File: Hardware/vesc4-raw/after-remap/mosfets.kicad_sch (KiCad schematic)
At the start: 15 parts, among them Q1 IPT007N06NATMA1, Q2 IPT007N06NATMA1, Q3 IPT007N06NATMA1, Q4 IPT007N06NATMA1, Q5 IPT007N06NATMA1, Q6 IPT007N06NATMA1

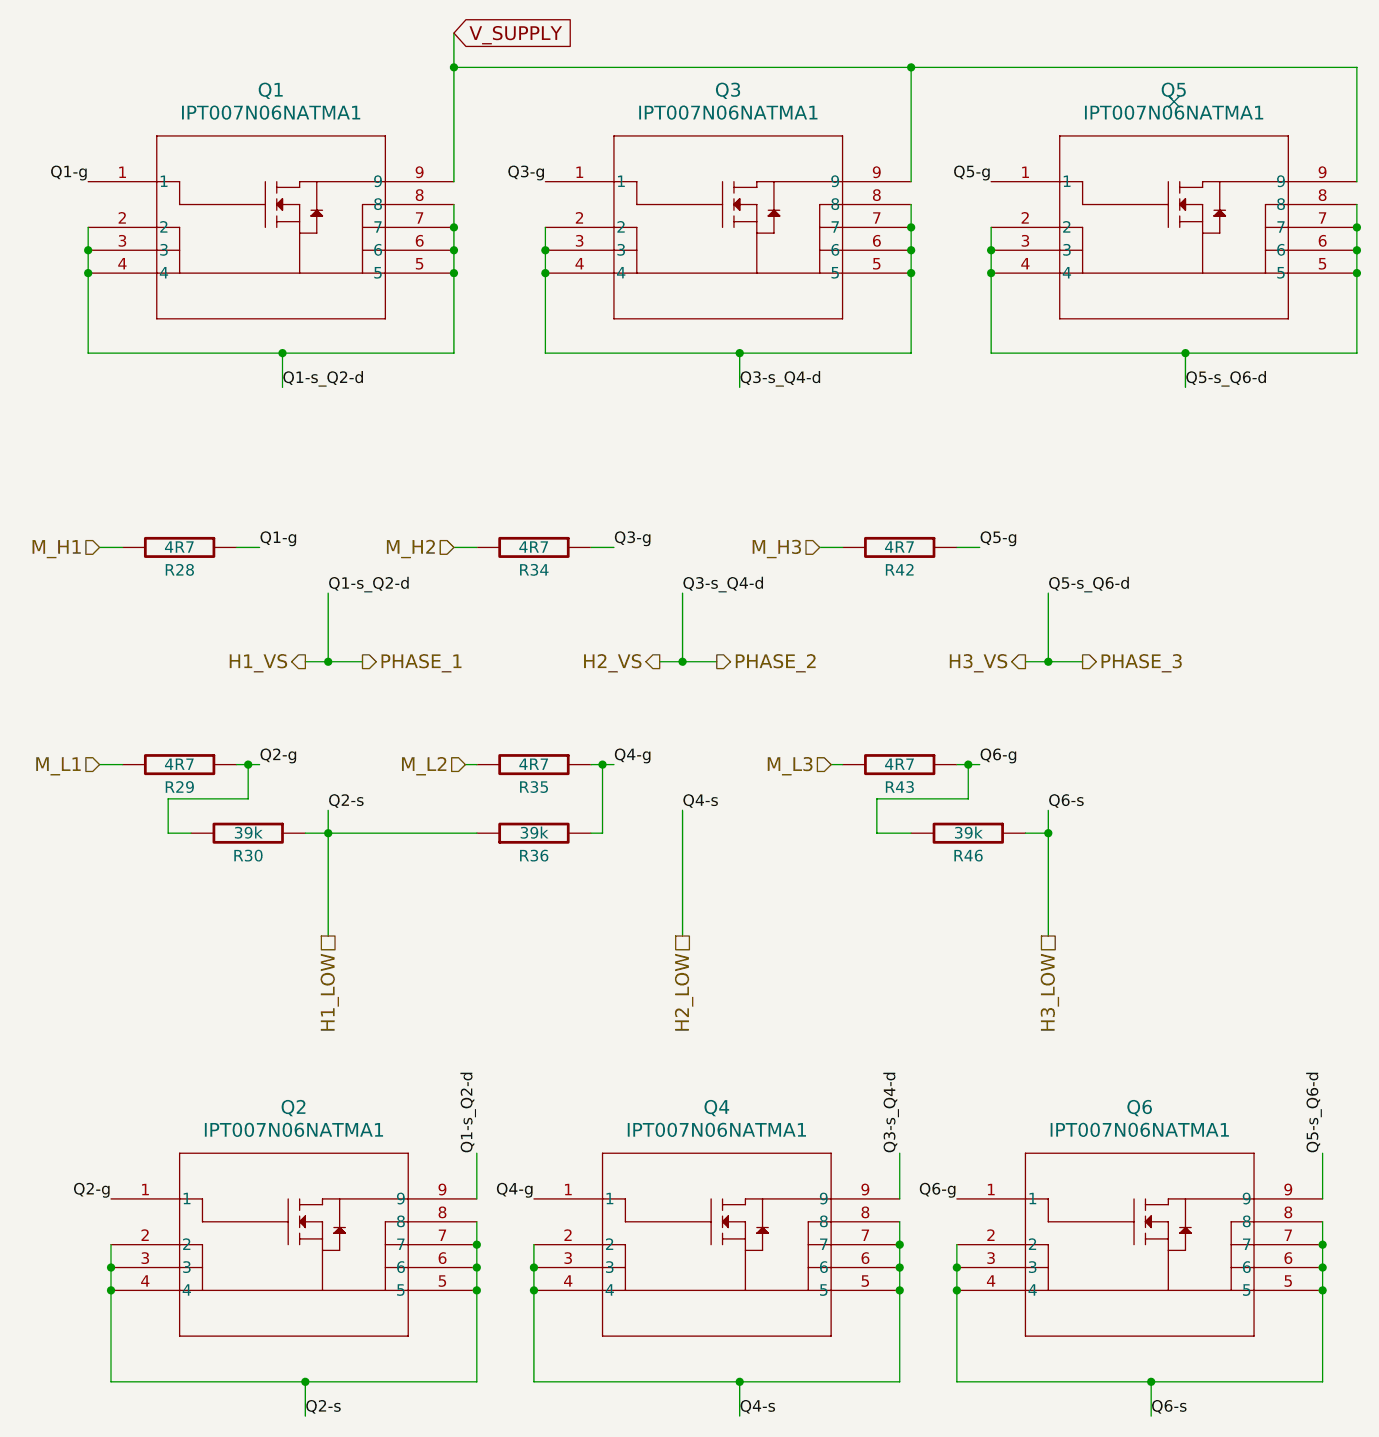
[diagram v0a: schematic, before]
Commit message: update mosfet
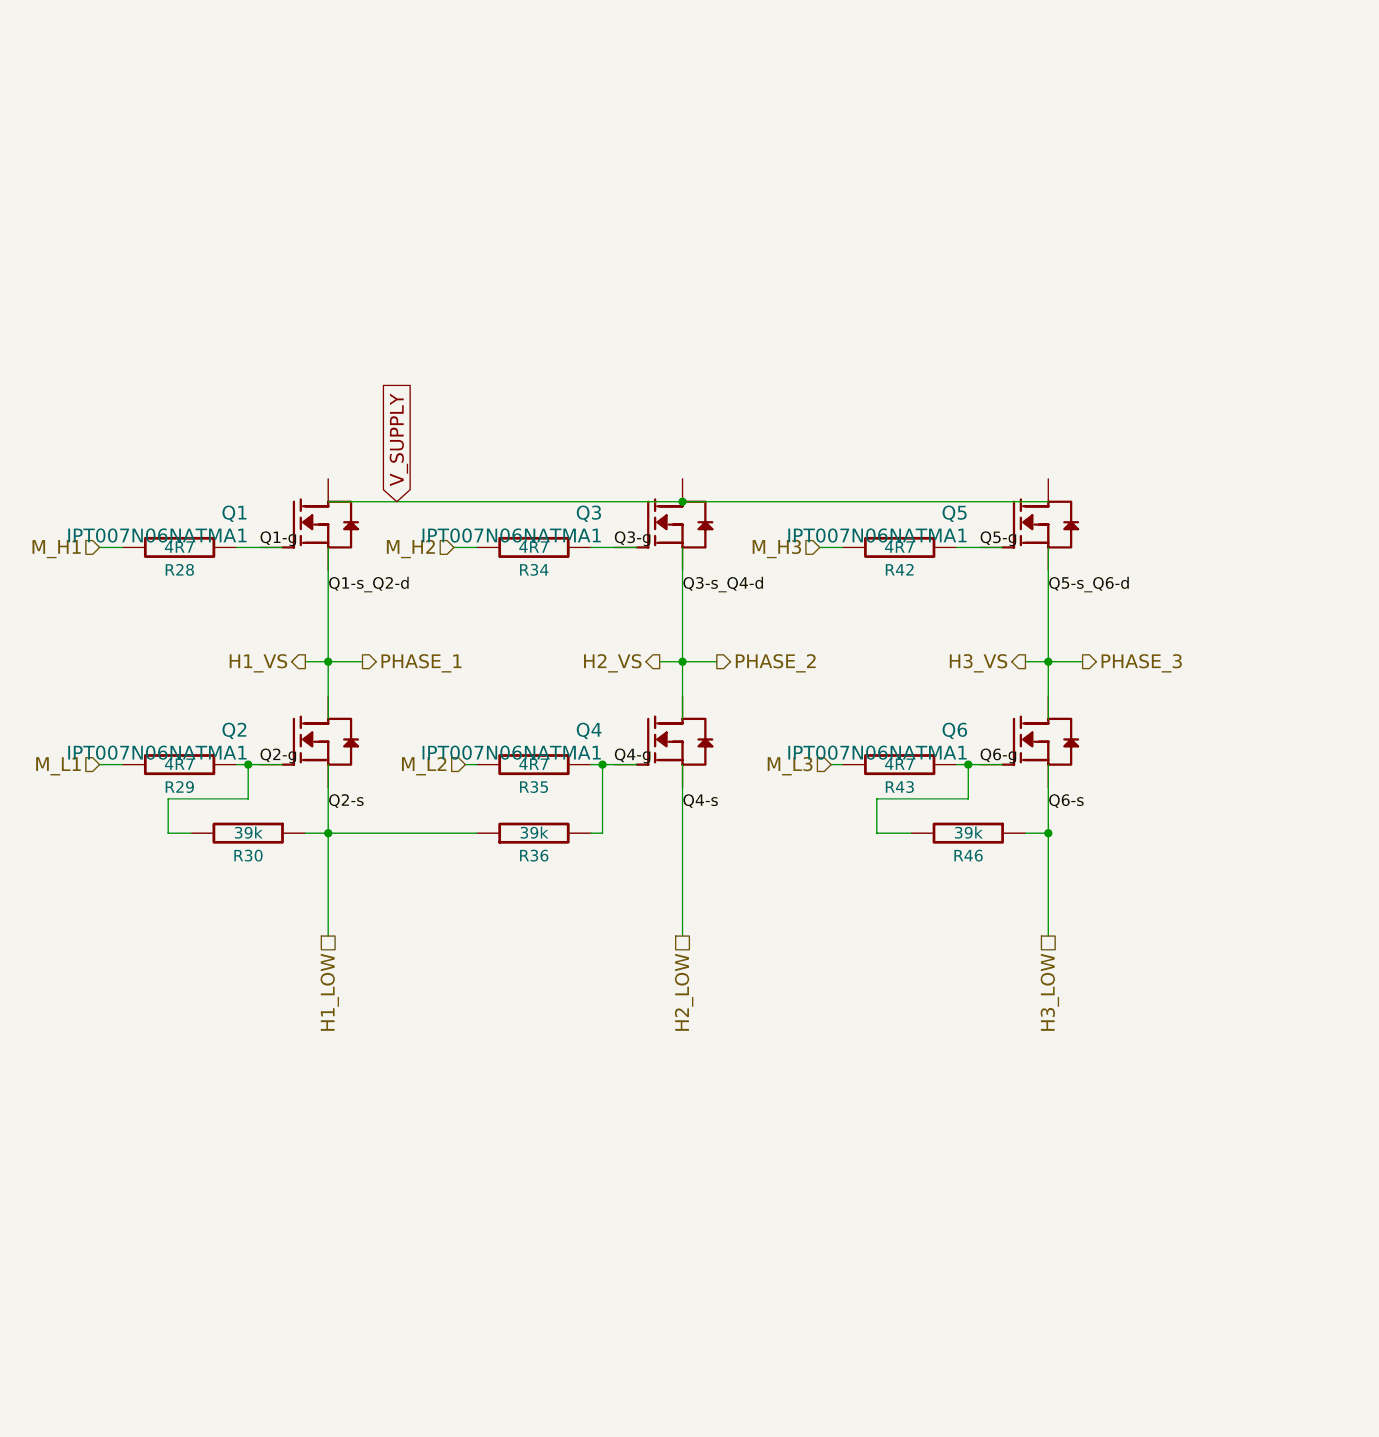
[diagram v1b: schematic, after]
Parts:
- Q1, Q2, Q3, Q4, Q5, Q6: symbol ipt007n06n:IPT007N06NATMA1 -> Library:IPT007N06N; Manufacturer (none) -> Infineon(英飞凌); Manufacturer Part (none) -> IPT007N06N; Supplier (none) -> LCSC; Supplier Part (none) -> C122552
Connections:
- net H1_LOW: no longer Q2.3, Q2.4, Q2.5, Q2.6, Q2.7, Q2.8
- net H1_VS: now also Q2.3 (D); no longer Q1.3, Q1.4, Q1.5, Q1.6, Q1.7, Q1.8, Q2.9
- net H2_LOW: no longer Q4.3, Q4.4, Q4.5, Q4.6, Q4.7, Q4.8
- net H2_VS: now also Q4.3 (D); no longer Q3.3, Q3.4, Q3.5, Q3.6, Q3.7, Q3.8, Q4.9
- net H3_LOW: no longer Q6.3, Q6.4, Q6.5, Q6.6, Q6.7, Q6.8
- net H3_VS: now also Q6.3 (D); no longer Q5.3, Q5.4, Q5.5, Q5.6, Q5.7, Q5.8, Q6.9
- net V_SUPPLY: now also Q1.3 (D), Q3.3 (D), Q5.3 (D); no longer Q1.9, Q3.9, Q5.9
- no-connect marks 1 -> 0

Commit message: chekcpoint 18 mei
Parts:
- Q1, Q2, Q3, Q4, Q5, Q6: footprint footprints:TRANS_IPT007N06NATMA1_INF-M -> easypretty:HSOF-8_IPT007N06N; JLC_3DModel (none) -> d50c126f5a2e4e8bb54a6100075e72a7; JLC_3D_Size (none) -> 9.9 11.675; LCSC (none) -> C122552; LCSC Part (none) -> C122552
- R28, R29, R34, R35, R42, R43: footprint Library:R0603 -> easypretty:R0603; LCSC (none) -> C23164; LCSC Part (none) -> C23164
- R30, R36, R46: footprint Library:R0603 -> easypretty:R0603; LCSC (none) -> C23153; LCSC Part (none) -> C23164

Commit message: 16-06-2026
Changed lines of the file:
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@@
 				)
 				(justify right)
+				(hide yes)
 			)
 		)
@@
 				)
 				(justify right)
+				(hide yes)
 			)
 		)
@@
 				)
 				(justify right)
+				(hide yes)
 			)
 		)
@@
 				)
 				(justify right)
+				(hide yes)
 			)
 		)
@@
 				)
 				(justify right)
+				(hide yes)
 			)
 		)
@@
 				)
 				(justify right)
-			)
-		)
+				(hide yes)
+			)
+		)
